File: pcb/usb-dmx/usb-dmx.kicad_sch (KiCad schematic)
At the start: 19 parts, among them J1 USB_C_Receptacle_USB2.0_16P, J2 USB_A, SW1 PTS526_SM15_SMTR2_LFS, U1 ESP32-S3-MINI-1U, U2 IP4234CZ6, U3 ADP2108AUJ-3.3, U4 ST485E

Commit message: adding receiving voltage divider and renaming components
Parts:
- added R5: 5k1, Resistor_SMD:R_0603_1608Metric_Pad0.98x0.95mm_HandSolder, symbol Device:R
- added R6: 10k, Resistor_SMD:R_0603_1608Metric_Pad0.98x0.95mm_HandSolder, symbol Device:R
- renumbered C7 to C3, C5 to C4, C3 to C5, R4 to R3, R3 to R4, U2 to U1, U3 to U2, U1 to U3
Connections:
- net 1: now also R5.1, R6.1; no longer U4.1 (RO)
- net GND: now also R6.2
- new net: R5.2, U4.1 (RO)
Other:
- title: TRANCE Devboard -> TRANCE USB-DMX
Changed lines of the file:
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@@
 	(paper "A3")
 	(title_block
-		(title "TRANCE Devboard")
+		(title "TRANCE USB-DMX")
 	)
 	(junction
@@
 	)
 	(junction
+		(at 214.63 205.74)
+		(diameter 0)
+		(color 0 0 0 0)
+	)
+	(junction
 		(at 321.31 208.28)
 		(diameter 0)
@@
 	(wire
 		(pts
+			(xy 214.63 195.58) (xy 214.63 194.31)
+		)
+		(stroke
+			(width 0)
+			(type default)
+		)
+	)
+	(wire
+		(pts
 			(xy 80.01 78.74) (xy 69.85 78.74)
 		)
@@
 	(wire
 		(pts
+			(xy 214.63 217.17) (xy 248.92 217.17)
+		)
+		(stroke
+			(width 0)
+			(type default)
+		)
+	)
+	(wire
+		(pts
 			(xy 232.41 204.47) (xy 238.76 204.47)
 		)
@@
 	(wire
 		(pts
+			(xy 214.63 203.2) (xy 214.63 205.74)
+		)
+		(stroke
+			(width 0)
+			(type default)
+		)
+	)
+	(wire
+		(pts
 			(xy 350.52 71.12) (xy 354.33 71.12)
 		)
@@
 	(wire
 		(pts
-			(xy 284.48 179.07) (xy 248.92 179.07)
+			(xy 214.63 215.9) (xy 214.63 217.17)
 		)
 		(stroke
@@
 	(wire
 		(pts
-			(xy 368.3 80.01) (xy 368.3 50.8)
+			(xy 284.48 179.07) (xy 248.92 179.07)
 		)
 		(stroke
@@
 	(wire
 		(pts
-			(xy 232.41 194.31) (xy 238.76 194.31)
+			(xy 368.3 80.01) (xy 368.3 50.8)
 		)
 		(stroke
@@
 	(wire
 		(pts
+			(xy 205.74 205.74) (xy 214.63 205.74)
+		)
+		(stroke
+			(width 0)
+			(type default)
+		)
+	)
+	(wire
+		(pts
 			(xy 77.47 71.12) (xy 77.47 73.66)
 		)
@@
 	(wire
 		(pts
+			(xy 214.63 194.31) (xy 238.76 194.31)
+		)
+		(stroke
+			(width 0)
+			(type default)
+		)
+	)
+	(wire
+		(pts
 			(xy 248.92 173.99) (xy 248.92 179.07)
 		)
@@
 	(wire
 		(pts
+			(xy 214.63 205.74) (xy 214.63 208.28)
+		)
+		(stroke
+			(width 0)
+			(type default)
+		)
+	)
+	(wire
+		(pts
 			(xy 203.2 69.85) (xy 203.2 73.66)
 		)
@@
 	)
 	(global_label "1"
-		(shape input)
-		(at 232.41 194.31 180)
+		(shape output)
+		(at 205.74 205.74 180)
 		(fields_autoplaced yes)
 		(effects
@@
 		)
 		(property "Intersheetrefs" "${INTERSHEET_REFS}"
-			(at 228.2153 194.31 0)
+			(at 201.5453 205.74 0)
 			(effects
 				(font
@@
 	)
 	(global_label "1"
-		(shape output)
+		(shape input)
 		(at 316.23 68.58 180)
 		(fields_autoplaced yes)
@@
 		(dnp no)
 		(fields_autoplaced yes)
-		(property "Reference" "R4"
+		(property "Reference" "R3"
 			(at 300.99 54.6099 0)
 			(effects
@@
 			(project "usb-dmx"
 				(path "/8846f2fa-8392-4ca0-b0ea-63a42c0612b6"
-					(reference "R4")
+					(reference "R3")
 					(unit 1)
 				)
@@
 		(dnp no)
 		(fields_autoplaced yes)
-		(property "Reference" "U2"
+		(property "Reference" "U1"
 			(at 124.46 67.31 0)
 			(effects
@@
 			(project ""
 				(path "/8846f2fa-8392-4ca0-b0ea-63a42c0612b6"
-					(reference "U2")
+					(reference "U1")
 					(unit 1)
 				)
@@
 		(dnp no)
 		(fields_autoplaced yes)
-		(property "Reference" "C7"
+		(property "Reference" "C3"
 			(at 302.26 66.0399 0)
 			(effects
@@
 			(project "usb-dmx"
 				(path "/8846f2fa-8392-4ca0-b0ea-63a42c0612b6"
-					(reference "C7")
+					(reference "C3")
 					(unit 1)
 				)
@@
 		(dnp no)
 		(fields_autoplaced yes)
-		(property "Reference" "U1"
+		(property "Reference" "U3"
 			(at 337.4233 53.34 0)
 			(effects
@@
 			(project ""
 				(path "/8846f2fa-8392-4ca0-b0ea-63a42c0612b6"
-					(reference "U1")
+					(reference "U3")
 					(unit 1)
 				)
@@
 		(dnp no)
 		(fields_autoplaced yes)
-		(property "Reference" "U3"
+		(property "Reference" "U2"
 			(at 220.98 60.96 0)
 			(effects
@@
 			(project ""
 				(path "/8846f2fa-8392-4ca0-b0ea-63a42c0612b6"
-					(reference "U3")
+					(reference "U2")
 					(unit 1)
 				)
@@
 	)
 	(symbol
+		(lib_id "Device:R")
+		(at 214.63 212.09 0)
+		(unit 1)
+		(exclude_from_sim no)
+		(in_bom yes)
+		(on_board yes)
+		(dnp no)
+		(fields_autoplaced yes)
+		(property "Reference" "R6"
+			(at 217.17 210.8199 0)
+			(effects
+				(font
+					(size 1.27 1.27)
+				)
+				(justify left)
+			)
+		)
+		(property "Value" "10k"
+			(at 217.17 213.3599 0)
+			(effects
+				(font
+					(size 1.27 1.27)
+				)
+				(justify left)
+			)
+		)
+		(property "Footprint" "Resistor_SMD:R_0603_1608Metric_Pad0.98x0.95mm_HandSolder"
+			(at 212.852 212.09 90)
+			(effects
+				(font
+					(size 1.27 1.27)
+				)
+				(hide yes)
+			)
+		)
+		(property "Datasheet" "~"
+			(at 214.63 212.09 0)
+			(effects
+				(font
+					(size 1.27 1.27)
+				)
+				(hide yes)
+			)
+		)
+		(property "Description" "Resistor"
+			(at 214.63 212.09 0)
+			(effects
+				(font
+					(size 1.27 1.27)
+				)
+				(hide yes)
+			)
+		)
+		(property "MOUSER_PART_NUMBER" "71-CRCW0402-10K-E3"
+			(at 214.63 212.09 0)
+			(effects
+				(font
+					(size 1.27 1.27)
+				)
+				(hide yes)
+			)
+		)
+		(pin "2"
+		)
+		(pin "1"
+		)
+		(instances
+			(project "usb-dmx"
+				(path "/8846f2fa-8392-4ca0-b0ea-63a42c0612b6"
+					(reference "R6")
+					(unit 1)
+				)
+			)
+		)
+	)
+	(symbol
 		(lib_id "Device:C")
 		(at 248.92 77.47 0)
@@
 		(dnp no)
 		(fields_autoplaced yes)
-		(property "Reference" "R3"
+		(property "Reference" "R4"
 			(at 140.97 187.9599 0)
 			(effects
@@
 			(project ""
 				(path "/8846f2fa-8392-4ca0-b0ea-63a42c0612b6"
-					(reference "R3")
+					(reference "R4")
 					(unit 1)
 				)
@@
 		(dnp no)
 		(fields_autoplaced yes)
-		(property "Reference" "C3"
+		(property "Reference" "C5"
 			(at 134.62 200.6599 0)
 			(effects
@@
 			(project ""
 				(path "/8846f2fa-8392-4ca0-b0ea-63a42c0612b6"
-					(reference "C3")
+					(reference "C5")
+					(unit 1)
+				)
+			)
+		)
+	)
+	(symbol
+		(lib_id "Device:R")
+		(at 214.63 199.39 180)
+		(unit 1)
+		(exclude_from_sim no)
+		(in_bom yes)
+		(on_board yes)
+		(dnp no)
+		(fields_autoplaced yes)
+		(property "Reference" "R5"
+			(at 217.17 198.1199 0)
+			(effects
+				(font
+					(size 1.27 1.27)
+				)
+				(justify right)
+			)
+		)
+		(property "Value" "5k1"
+			(at 217.17 200.6599 0)
+			(effects
+				(font
+					(size 1.27 1.27)
+				)
+				(justify right)
+			)
+		)
+		(property "Footprint" "Resistor_SMD:R_0603_1608Metric_Pad0.98x0.95mm_HandSolder"
+			(at 216.408 199.39 90)
+			(effects
+				(font
+					(size 1.27 1.27)
+				)
+				(hide yes)
+			)
+		)
+		(property "Datasheet" "~"
+			(at 214.63 199.39 0)
+			(effects
+				(font
+					(size 1.27 1.27)
+				)
+				(hide yes)
+			)
+		)
+		(property "Description" "Resistor"
+			(at 214.63 199.39 0)
+			(effects
+				(font
+					(size 1.27 1.27)
+				)
+				(hide yes)
+			)
+		)
+		(property "MOUSER_PART_NUMBER" "71-CRCW0402-5.1K-E3"
+			(at 214.63 199.39 0)
+			(effects
+				(font
+					(size 1.27 1.27)
+				)
+				(hide yes)
+			)
+		)
+		(pin "2"
+		)
+		(pin "1"
+		)
+		(instances
+			(project "usb-dmx"
+				(path "/8846f2fa-8392-4ca0-b0ea-63a42c0612b6"
+					(reference "R5")
 					(unit 1)
 				)
@@
 		(dnp no)
 		(fields_autoplaced yes)
-		(property "Reference" "C5"
+		(property "Reference" "C4"
 			(at 372.11 82.5499 0)
 			(effects
@@
 			(project "devboard"
 				(path "/8846f2fa-8392-4ca0-b0ea-63a42c0612b6"
-					(reference "C5")
+					(reference "C4")
 					(unit 1)
 				)

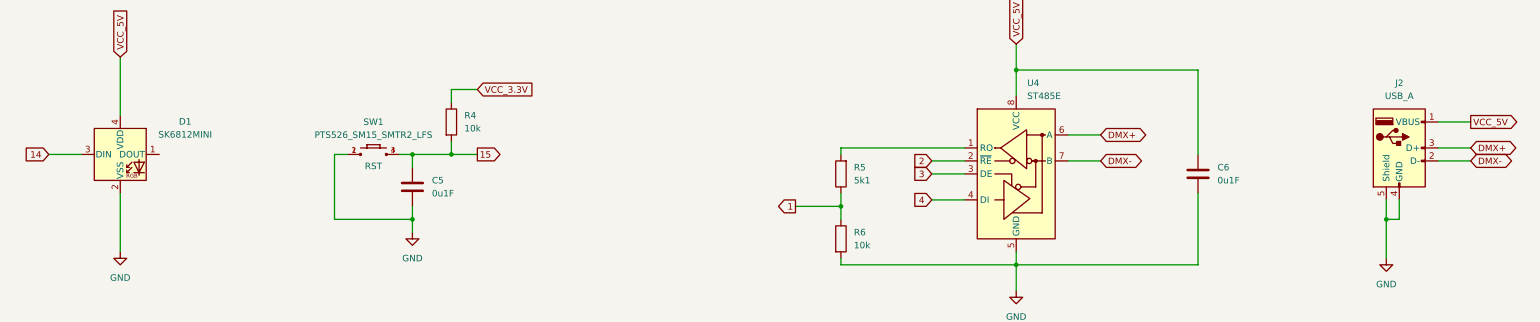
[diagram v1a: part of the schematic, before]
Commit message: preparing usb-dmx for production
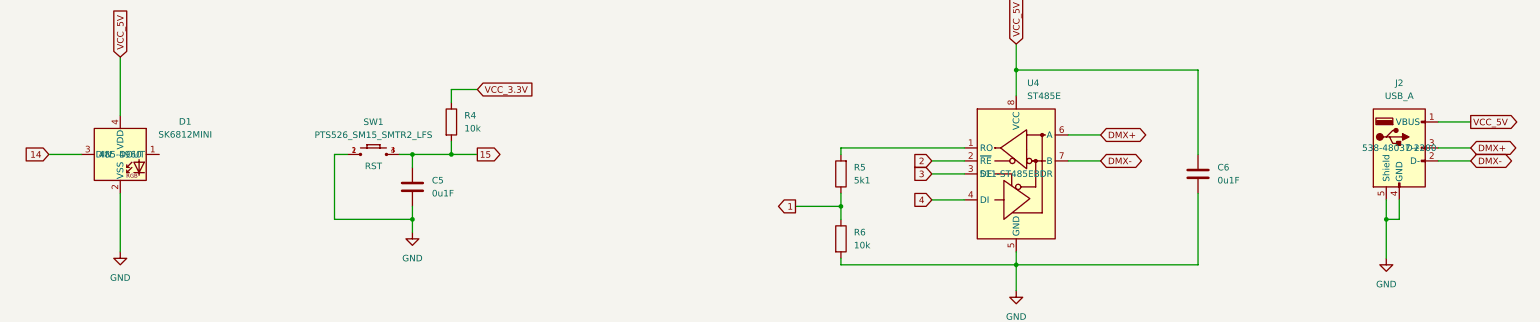
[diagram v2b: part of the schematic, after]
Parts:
- C1: MOUSER_PART_NUMBER 187-CL10A475KO8NNNC -> 187-CL10A475KP8NNWC
- C3: MOUSER_PART_NUMBER 187-CL05F104ZO5NNND -> 187-CL10B105KA8NNND
- C4, C5, C6: MOUSER_PART_NUMBER 187-CL05F104ZO5NNND -> 187-CL10B104KA8NNNC
- D1: MOUSER_PART_NUMBER (none) -> 485-4960
- J1: MOUSER_PART_NUMBER (none) -> 640-USB4110-GF-A
- J2: MOUSER_PART_NUMBER (none) -> 538-48037-2200
- R1, R2, R5: MOUSER_PART_NUMBER 71-CRCW0402-5.1K-E3 -> 71-CRCW0603-5.1K-E3
- R3, R4, R6: MOUSER_PART_NUMBER 71-CRCW0402-10K-E3 -> 71-CRCW0603-10K-E3
- U4: MOUSER_PART_NUMBER (none) -> 511-ST485EBDR
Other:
- company: (none) -> Author: Samuel Hafen
- title: TRANCE USB-DMX -> USB-DMX
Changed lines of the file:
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@@
 	(paper "A3")
 	(title_block
-		(title "TRANCE USB-DMX")
+		(title "USB-DMX")
+		(rev "1")
+		(company "Author: Samuel Hafen")
 	)
 	(junction
@@
 			)
 		)
-		(property "MOUSER_PART_NUMBER" "71-CRCW0402-10K-E3"
+		(property "MOUSER_PART_NUMBER" "71-CRCW0603-10K-E3"
 			(at 298.45 55.88 0)
 			(effects
@@
 			)
 		)
+		(property "DigiKey_Part_Number" ""
+			(at 298.45 55.88 0)
+			(effects
+				(font
+					(size 1.27 1.27)
+				)
+			)
+		)
 		(pin "2"
 		)
@@
 			)
 		)
+		(property "DigiKey_Part_Number" ""
+			(at 248.92 199.39 0)
+			(effects
+				(font
+					(size 1.27 1.27)
+				)
+			)
+		)
+		(property "MOUSER_PART_NUMBER" "511-ST485EBDR"
+			(at 248.92 199.39 0)
+			(effects
+				(font
+					(size 1.27 1.27)
+				)
+			)
+		)
 		(pin "7"
 		)
@@
 			)
 		)
+		(property "DigiKey_Part_Number" ""
+			(at 118.11 73.66 0)
+			(effects
+				(font
+					(size 1.27 1.27)
+				)
+			)
+		)
 		(pin "2"
 		)
@@
 			)
 		)
-		(property "MOUSER_PART_NUMBER" "71-CRCW0402-5.1K-E3"
+		(property "MOUSER_PART_NUMBER" "71-CRCW0603-5.1K-E3"
 			(at 82.55 63.5 0)
 			(effects
@@
 			)
 		)
+		(property "DigiKey_Part_Number" ""
+			(at 82.55 63.5 0)
+			(effects
+				(font
+					(size 1.27 1.27)
+				)
+			)
+		)
 		(pin "2"
 		)
@@
 			)
 		)
-		(property "MOUSER_PART_NUMBER" "187-CL05F104ZO5NNND"
+		(property "MOUSER_PART_NUMBER" "187-CL10B105KA8NNND"
 			(at 298.45 67.31 0)
 			(effects
@@
 			)
 		)
+		(property "DigiKey_Part_Number" ""
+			(at 298.45 67.31 0)
+			(effects
+				(font
+					(size 1.27 1.27)
+				)
+			)
+		)
 		(pin "1"
 		)
@@
 			)
 		)
+		(property "DigiKey_Part_Number" ""
+			(at 234.95 69.85 0)
+			(effects
+				(font
+					(size 1.27 1.27)
+				)
+			)
+		)
 		(pin "2"
 		)
@@
 			)
 		)
+		(property "DigiKey_Part_Number" ""
+			(at 335.28 86.36 0)
+			(effects
+				(font
+					(size 1.27 1.27)
+				)
+			)
+		)
 		(pin "62"
 		)
@@
 			)
 		)
+		(property "DigiKey_Part_Number" ""
+			(at 123.19 195.58 0)
+			(effects
+				(font
+					(size 1.27 1.27)
+				)
+			)
+		)
 		(pin "2"
 		)
@@
 			)
 		)
+		(property "MOUSER_PART_NUMBER" "640-USB4110-GF-A"
+			(at 54.61 73.66 0)
+			(effects
+				(font
+					(size 1.27 1.27)
+				)
+				(hide yes)
+			)
+		)
+		(property "DigiKey_Part_Number" ""
+			(at 54.61 73.66 0)
+			(effects
+				(font
+					(size 1.27 1.27)
+				)
+			)
+		)
 		(pin "A1"
 		)
@@
 			)
 		)
-		(property "MOUSER_PART_NUMBER" "187-CL05F104ZO5NNND"
+		(property "MOUSER_PART_NUMBER" "187-CL10B104KA8NNNC"
 			(at 284.48 199.39 0)
 			(effects
@@
 			)
 		)
+		(property "DigiKey_Part_Number" ""
+			(at 284.48 199.39 0)
+			(effects
+				(font
+					(size 1.27 1.27)
+				)
+			)
+		)
 		(pin "1"
 		)
@@
 			)
 		)
+		(property "DigiKey_Part_Number" ""
+			(at 220.98 72.39 0)
+			(effects
+				(font
+					(size 1.27 1.27)
+				)
+			)
+		)
 		(pin "1"
 		)
@@
 			)
 		)
+		(property "DigiKey_Part_Number" ""
+			(at 73.66 195.58 0)
+			(effects
+				(font
+					(size 1.27 1.27)
+				)
+			)
+		)
+		(property "MOUSER_PART_NUMBER" "485-4960"
+			(at 73.66 195.58 0)
+			(effects
+				(font
+					(size 1.27 1.27)
+				)
+			)
+		)
 		(pin "3"
 		)
@@
 			)
 		)
-		(property "MOUSER_PART_NUMBER" "71-CRCW0402-5.1K-E3"
+		(property "MOUSER_PART_NUMBER" "71-CRCW0603-5.1K-E3"
 			(at 76.2 66.04 0)
 			(effects
@@
 			)
 		)
+		(property "DigiKey_Part_Number" ""
+			(at 76.2 66.04 0)
+			(effects
+				(font
+					(size 1.27 1.27)
+				)
+			)
+		)
 		(pin "2"
 		)
@@
 			)
 		)
-		(property "MOUSER_PART_NUMBER" "71-CRCW0402-10K-E3"
+		(property "MOUSER_PART_NUMBER" "71-CRCW0603-10K-E3"
 			(at 214.63 212.09 0)
 			(effects
@@
 			)
 		)
+		(property "DigiKey_Part_Number" ""
+			(at 214.63 212.09 0)
+			(effects
+				(font
+					(size 1.27 1.27)
+				)
+			)
+		)
 		(pin "2"
 		)
@@
 			)
 		)
+		(property "DigiKey_Part_Number" ""
+			(at 248.92 77.47 0)
+			(effects
+				(font
+					(size 1.27 1.27)
+				)
+			)
+		)
 		(pin "2"
 		)
@@
 			)
 		)
-		(property "Datasheet" "~"
+		(property "Datasheet" "https://www.molex.com/en-us/products/part-detail-pdf/480372200?display=pdf"
 			(at 327.66 195.58 0)
 			(effects
@@
 			)
 		)
+		(property "DigiKey_Part_Number" ""
+			(at 323.85 194.31 0)
+			(effects
+				(font
+					(size 1.27 1.27)
+				)
+			)
+		)
+		(property "MOUSER_PART_NUMBER" "538-48037-2200"
+			(at 323.85 194.31 0)
+			(effects
+				(font
+					(size 1.27 1.27)
+				)
+			)
+		)
 		(pin "2"
 		)
@@
 			)
 		)
-		(property "MOUSER_PART_NUMBER" "187-CL10A475KO8NNNC"
+		(property "MOUSER_PART_NUMBER" "187-CL10A475KP8NNWC"
 			(at 203.2 77.47 0)
 			(effects
@@
 			)
 		)
+		(property "DigiKey_Part_Number" ""
+			(at 203.2 77.47 0)
+			(effects
+				(font
+					(size 1.27 1.27)
+				)
+			)
+		)
 		(pin "2"
 		)
@@
 			)
 		)
-		(property "MOUSER_PART_NUMBER" "71-CRCW0402-10K-E3"
+		(property "MOUSER_PART_NUMBER" "71-CRCW0603-10K-E3"
 			(at 138.43 189.23 0)
 			(effects
@@
 			)
 		)
+		(property "DigiKey_Part_Number" ""
+			(at 138.43 189.23 0)
+			(effects
+				(font
+					(size 1.27 1.27)
+				)
+			)
+		)
 		(pin "2"
 		)
@@
 			)
 		)
-		(property "MOUSER_PART_NUMBER" "187-CL05F104ZO5NNND"
+		(property "MOUSER_PART_NUMBER" "187-CL10B104KA8NNNC"
 			(at 130.81 201.93 0)
 			(effects
@@
 			)
 		)
+		(property "DigiKey_Part_Number" ""
+			(at 130.81 201.93 0)
+			(effects
+				(font
+					(size 1.27 1.27)
+				)
+			)
+		)
 		(pin "1"
 		)
@@
 			)
 		)
-		(property "MOUSER_PART_NUMBER" "71-CRCW0402-5.1K-E3"
+		(property "MOUSER_PART_NUMBER" "71-CRCW0603-5.1K-E3"
 			(at 214.63 199.39 0)
 			(effects
@@
 			)
 		)
+		(property "DigiKey_Part_Number" ""
+			(at 214.63 199.39 0)
+			(effects
+				(font
+					(size 1.27 1.27)
+				)
+			)
+		)
 		(pin "2"
 		)
@@
 			)
 		)
-		(property "MOUSER_PART_NUMBER" "187-CL05F104ZO5NNND"
+		(property "MOUSER_PART_NUMBER" "187-CL10B104KA8NNNC"
 			(at 368.3 83.82 0)
 			(effects
@@
 			)
 		)
+		(property "DigiKey_Part_Number" ""
+			(at 368.3 83.82 0)
+			(effects
+				(font
+					(size 1.27 1.27)
+				)
+			)
+		)
